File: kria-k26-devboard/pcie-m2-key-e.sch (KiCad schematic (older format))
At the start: 10 parts, among them P1 2199119-6

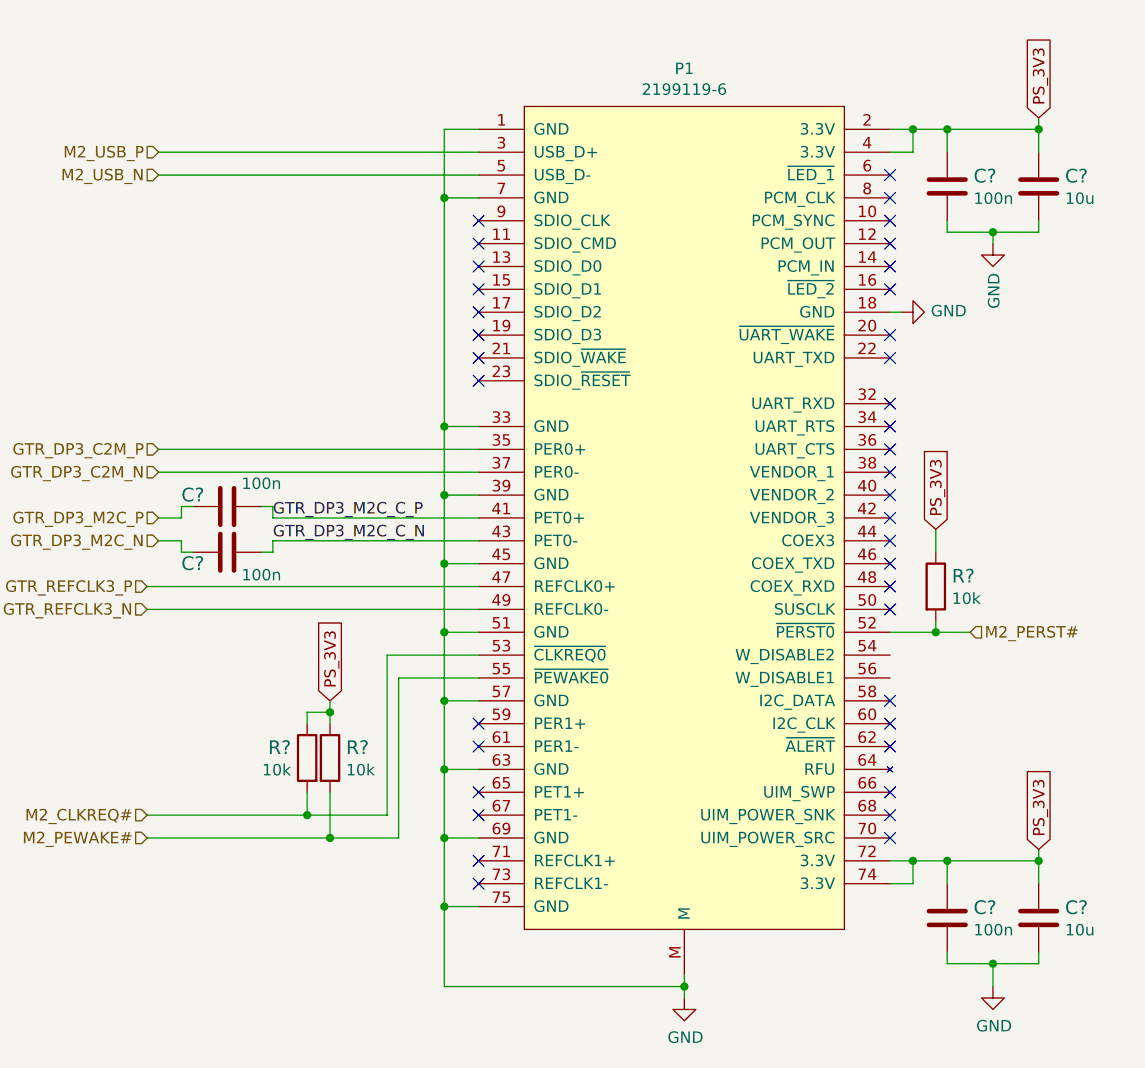
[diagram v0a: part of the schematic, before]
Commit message: Finished reset logic, added crystal gen. to USB PHY, create power toggle for SD 3.0
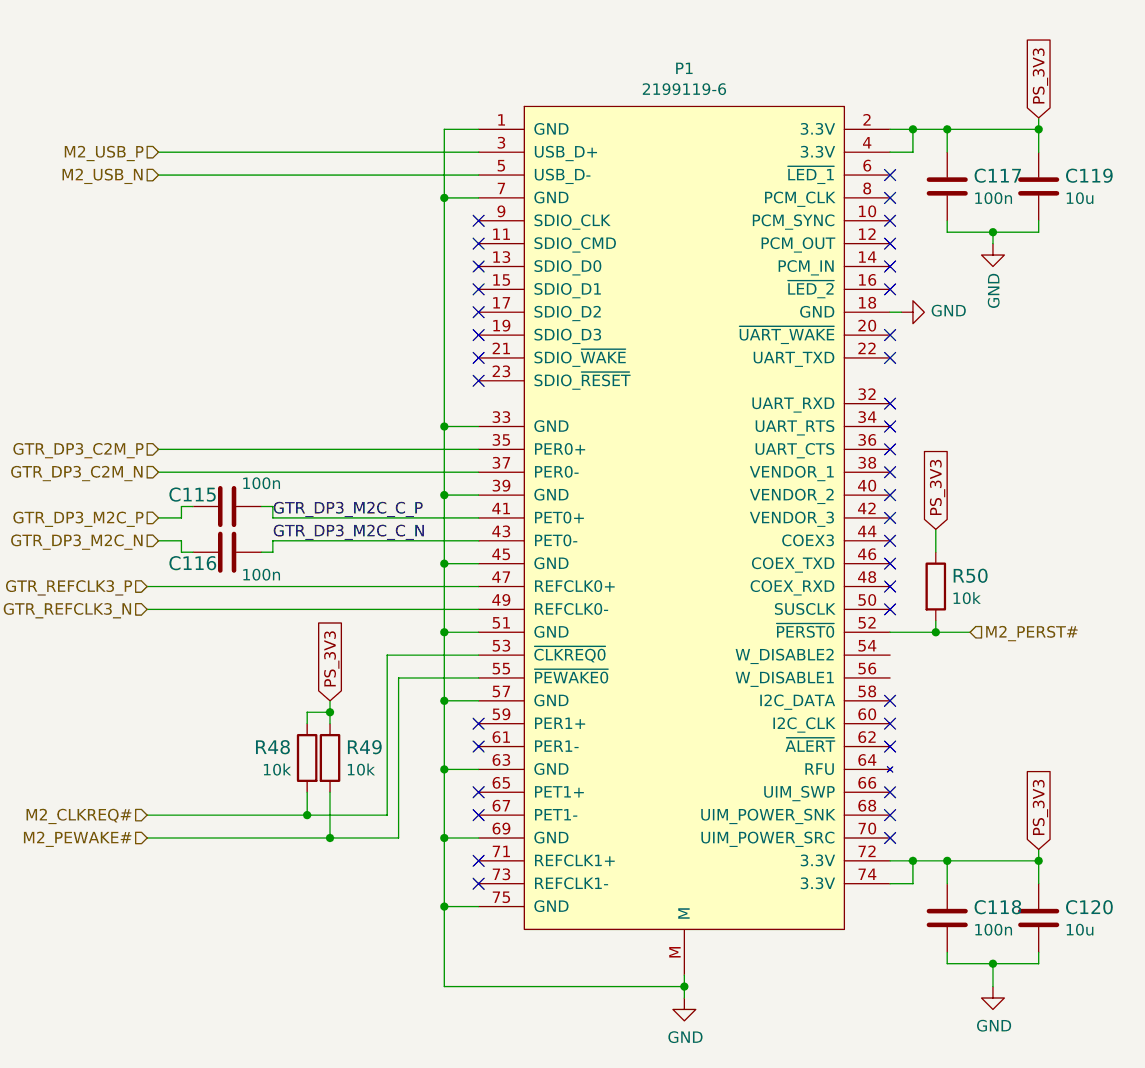
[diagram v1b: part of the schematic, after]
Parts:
- gave numbers to parts that had none: 9
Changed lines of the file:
@@
 Connection ~ 4950 5100
 $Comp
-L power:GND #PWR?
+L power:GND #PWR069
 U 1 1 65600FFC
 P 6000 5500
-F 0 "#PWR?" H 6000 5250 50  0001 C CNN
+F 0 "#PWR069" H 6000 5250 50  0001 C CNN
 F 1 "GND" H 6005 5327 50  0000 C CNN
 F 2 "" H 6000 5500 50  0001 C CNN
@@
 NoConn ~ 6900 4200
 $Comp
-L antmicroCapacitors0402:C_100n_0402 C?
+L antmicroCapacitors0402:C_100n_0402 C115
 U 1 1 65611557
 P 4000 3350
-F 0 "C?" V 3950 3200 60  0000 C CNN
+F 0 "C115" V 3950 3200 60  0000 C CNN
 F 1 "C_100n_0402" H 4000 3200 60  0001 C CNN
 F 2 "antmicro-footprints:0402-cap" H 4200 3550 60  0001 L CNN
@@
 $EndComp
 $Comp
-L antmicroCapacitors0402:C_100n_0402 C?
+L antmicroCapacitors0402:C_100n_0402 C116
 U 1 1 656118CD
 P 4000 3550
-F 0 "C?" V 3950 3400 60  0000 C CNN
+F 0 "C116" V 3950 3400 60  0000 C CNN
 F 1 "C_100n_0402" H 4000 3400 60  0001 C CNN
 F 2 "antmicro-footprints:0402-cap" H 4200 3750 60  0001 L CNN
@@
 PS_3V3
 $Comp
-L antmicroCapacitors0603:C_10u_0603 C?
+L antmicroCapacitors0603:C_10u_0603 C119
 U 1 1 65686406
 P 7550 1950
-F 0 "C?" H 7665 1995 60  0000 L CNN
+F 0 "C119" H 7665 1995 60  0000 L CNN
 F 1 "C_10u_0603" H 7550 1800 60  0001 C CNN
 F 2 "antmicro-footprints:0603-cap" H 7750 2150 60  0001 L CNN
@@
 PS_3V3
 $Comp
-L antmicroResistors0402:R_10k_0402 R?
+L antmicroResistors0402:R_10k_0402 R49
 U 1 1 6569DB94
 P 4450 4450
-F 0 "R?" V 4405 4520 60  0000 L CNN
+F 0 "R49" V 4405 4520 60  0000 L CNN
 F 1 "R_10k_0402" H 4450 4300 60  0001 C CNN
 F 2 "antmicro-footprints:0402-res" H 4650 4650 60  0001 L CNN
@@
 $EndComp
 $Comp
-L antmicroResistors0402:R_10k_0402 R?
+L antmicroResistors0402:R_10k_0402 R48
 U 1 1 6569F2E0
 P 4350 4450
-F 0 "R?" V 4305 4520 60  0000 L CNN
+F 0 "R48" V 4305 4520 60  0000 L CNN
 F 1 "R_10k_0402" H 4350 4300 60  0001 C CNN
 F 2 "antmicro-footprints:0402-res" H 4550 4650 60  0001 L CNN
@@
 M2_PEWAKE#
 $Comp
-L antmicroResistors0402:R_10k_0402 R?
+L antmicroResistors0402:R_10k_0402 R50
 U 1 1 656A5E34
 P 7100 3700
-F 0 "R?" V 7055 3770 60  0000 L CNN
+F 0 "R50" V 7055 3770 60  0000 L CNN
 F 1 "R_10k_0402" H 7100 3550 60  0001 C CNN
 F 2 "antmicro-footprints:0402-res" H 7300 3900 60  0001 L CNN
@@
 Connection ~ 7000 1700
 $Comp
-L antmicroCapacitors0402:C_100n_0402 C?
+L antmicroCapacitors0402:C_100n_0402 C117
 U 1 1 656D8EC8
 P 7150 1950
-F 0 "C?" H 7265 1995 60  0000 L CNN
+F 0 "C117" H 7265 1995 60  0000 L CNN
 F 1 "C_100n_0402" H 7150 1800 60  0001 C CNN
 F 2 "antmicro-footprints:0402-cap" H 7350 2150 60  0001 L CNN
@@
 PS_3V3
 $Comp
-L antmicroCapacitors0603:C_10u_0603 C?
+L antmicroCapacitors0603:C_10u_0603 C120
 U 1 1 656DBDBC
 P 7550 5150
-F 0 "C?" H 7665 5195 60  0000 L CNN
+F 0 "C120" H 7665 5195 60  0000 L CNN
 F 1 "C_10u_0603" H 7550 5000 60  0001 C CNN
 F 2 "antmicro-footprints:0603-cap" H 7750 5350 60  0001 L CNN
@@
 Connection ~ 7550 4900
 $Comp
-L power:GND #PWR?
+L power:GND #PWR072
 U 1 1 656DBDCA
 P 7350 5450
-F 0 "#PWR?" H 7350 5200 50  0001 C CNN
+F 0 "#PWR072" H 7350 5200 50  0001 C CNN
 F 1 "GND" H 7355 5277 50  0000 C CNN
 F 2 "" H 7350 5450 50  0001 C CNN
@@
 	7550 4900 7550 4850
 $Comp
-L antmicroCapacitors0402:C_100n_0402 C?
+L antmicroCapacitors0402:C_100n_0402 C118
 U 1 1 656DBDDE
 P 7150 5150
-F 0 "C?" H 7265 5195 60  0000 L CNN
+F 0 "C118" H 7265 5195 60  0000 L CNN
 F 1 "C_100n_0402" H 7150 5000 60  0001 C CNN
 F 2 "antmicro-footprints:0402-cap" H 7350 5350 60  0001 L CNN
@@
 Connection ~ 7150 1700
 $Comp
-L power:GND #PWR?
+L power:GND #PWR071
 U 1 1 656CB469
 P 7350 2200
-F 0 "#PWR?" H 7350 1950 50  0001 C CNN
+F 0 "#PWR071" H 7350 1950 50  0001 C CNN
 F 1 "GND" V 7355 2072 50  0000 R CNN
 F 2 "" H 7350 2200 50  0001 C CNN
@@
 	7350 2150 7550 2150
 $Comp
-L power:GND #PWR?
+L power:GND #PWR070
 U 1 1 657BC2E7
 P 6950 2500
-F 0 "#PWR?" H 6950 2250 50  0001 C CNN
+F 0 "#PWR070" H 6950 2250 50  0001 C CNN
 F 1 "GND" V 6955 2372 50  0000 R CNN
 F 2 "" H 6950 2500 50  0001 C CNN

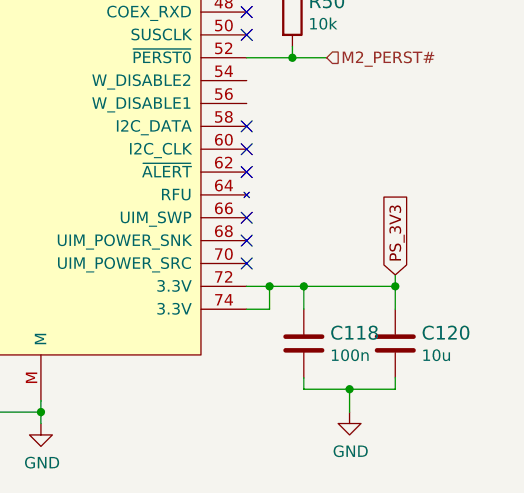
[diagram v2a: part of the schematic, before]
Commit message: Added second ETH interface, connect POE PSE
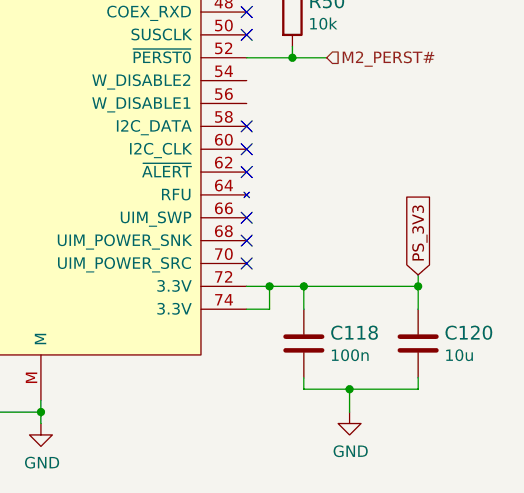
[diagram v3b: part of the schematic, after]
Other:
- moved on the sheet: C120
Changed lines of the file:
@@
 	1    0    0    -1
 $EndComp
-Text GLabel 7550 4850 1    50   Input ~ 0
+Text GLabel 7650 4850 1    50   Input ~ 0
 PS_3V3
 $Comp
 L antmicroCapacitors0603:C_10u_0603 C120
 U 1 1 656DBDBC
-P 7550 5150
-F 0 "C120" H 7665 5195 60  0000 L CNN
-F 1 "C_10u_0603" H 7550 5000 60  0001 C CNN
-F 2 "antmicro-footprints:0603-cap" H 7750 5350 60  0001 L CNN
-F 3 "" H 7550 5150 50  0001 C CNN
-F 4 "Murata" H 7750 5550 60  0001 L CNN "Manufacturer"
-F 5 "GRM188R61A106KE69D" H 7750 5450 60  0001 L CNN "MPN"
-F 6 "10u" H 7665 5097 50  0000 L CNN "Val"
-	1    7550 5150
+P 7650 5150
+F 0 "C120" H 7765 5195 60  0000 L CNN
+F 1 "C_10u_0603" H 7650 5000 60  0001 C CNN
+F 2 "antmicro-footprints:0603-cap" H 7850 5350 60  0001 L CNN
+F 3 "" H 7650 5150 50  0001 C CNN
+F 4 "Murata" H 7850 5550 60  0001 L CNN "Manufacturer"
+F 5 "GRM188R61A106KE69D" H 7850 5450 60  0001 L CNN "MPN"
+F 6 "10u" H 7765 5097 50  0000 L CNN "Val"
+	1    7650 5150
 	1    0    0    -1
 $EndComp
@@
 	7150 5000 7150 4900
 Wire Wire Line
-	7150 4900 7550 4900
+	7150 4900 7650 4900
 Wire Wire Line
-	7550 4900 7550 5000
-Connection ~ 7550 4900
+	7650 4900 7650 5000
+Connection ~ 7650 4900
 $Comp
 L power:GND #PWR072
@@
 	7150 5350 7350 5350
 Wire Wire Line
-	7550 5350 7550 5300
+	7650 5350 7650 5300
 Wire Wire Line
 	7350 5450 7350 5350
 Connection ~ 7350 5350
 Wire Wire Line
-	7350 5350 7550 5350
+	7350 5350 7650 5350
 Wire Wire Line
-	7550 4900 7550 4850
+	7650 4900 7650 4850
 $Comp
 L antmicroCapacitors0402:C_100n_0402 C118

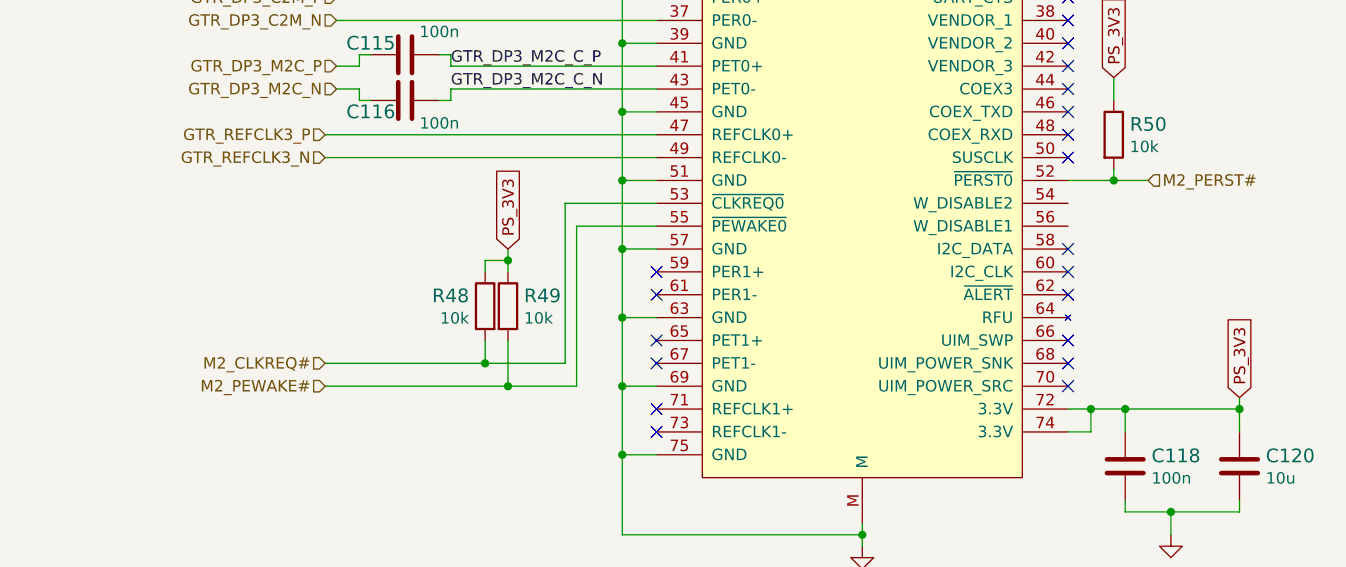
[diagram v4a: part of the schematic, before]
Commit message: fixed an issue with reset logic (Mixed PS and PL domain on OD buffer), extended the logic circuit to support M.2 PERST# (reset for PCIe WIFI), fixed the polarity of the camera control signal CAM_RST to comply with Antmicro standard, change CAM _SHDN to CAM_VSYNC, replaced the reset connector to fit additional signal M2_PERST
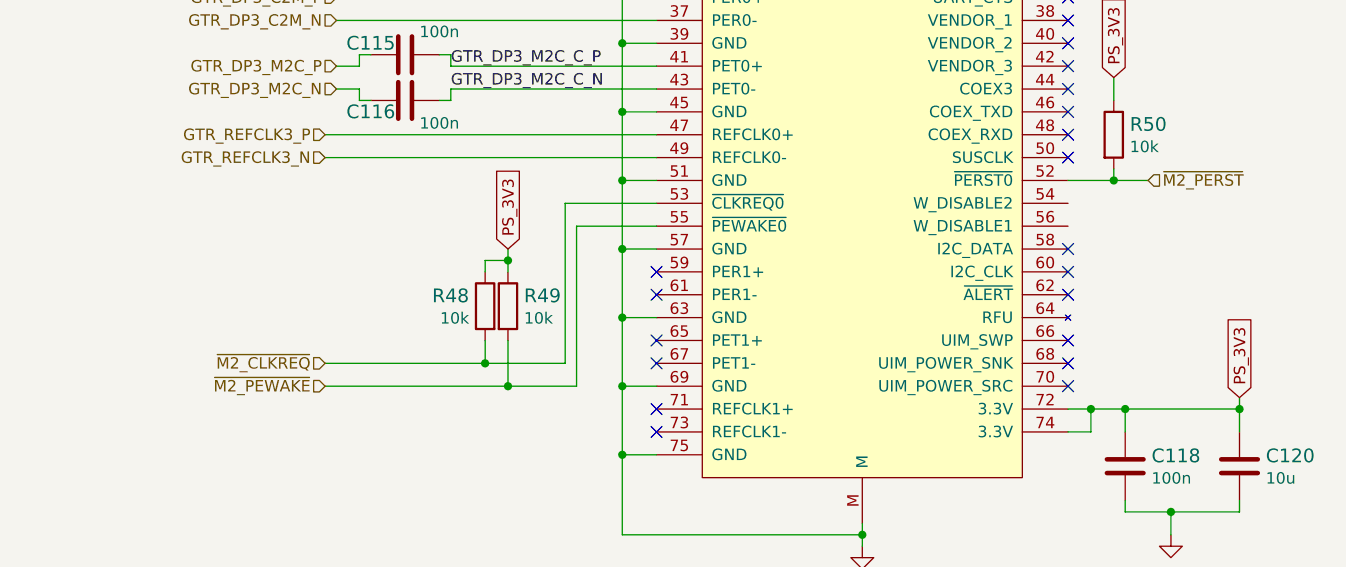
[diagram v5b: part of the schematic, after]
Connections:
- net M2_CLKREQ# renamed ~M2_CLKREQ
- net M2_PERST# renamed ~M2_PERST
- net M2_PEWAKE# renamed ~M2_PEWAKE
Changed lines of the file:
@@
 Wire Wire Line
 	4450 4600 4450 4800
-Text HLabel 3650 4700 0    50   Input ~ 0
-M2_CLKREQ#
 Text HLabel 3650 4800 0    50   Input ~ 0
-M2_PEWAKE#
+~M2_PEWAKE
 $Comp
 L antmicroResistors0402:R_10k_0402 R50
@@
 	7100 3550 7100 3450
 Text HLabel 7250 3900 2    50   Input ~ 0
-M2_PERST#
+~M2_PERST
 Wire Wire Line
 	7100 3900 7250 3900
@@
 	6000 5500 6000 5450
 Connection ~ 6000 5450
+Text HLabel 3650 4700 0    50   Input ~ 0
+~M2_CLKREQ
 $EndSCHEMATC

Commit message: Progress in PCB placement
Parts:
- renumbered C115 to C1, C116 to C2, C117 to C3, C118 to C4, C119 to C5, C120 to C6, R48 to R1, R49 to R2, R50 to R3
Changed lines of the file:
@@
 Connection ~ 4950 5100
 $Comp
-L power:GND #PWR069
+L power:GND #PWR01
 U 1 1 65600FFC
 P 6000 5500
-F 0 "#PWR069" H 6000 5250 50  0001 C CNN
+F 0 "#PWR01" H 6000 5250 50  0001 C CNN
 F 1 "GND" H 6005 5327 50  0000 C CNN
 F 2 "" H 6000 5500 50  0001 C CNN
@@
 NoConn ~ 6900 4200
 $Comp
-L antmicroCapacitors0402:C_100n_0402 C115
+L antmicroCapacitors0402:C_100n_0402 C1
 U 1 1 65611557
 P 4000 3350
-F 0 "C115" V 3950 3200 60  0000 C CNN
+F 0 "C1" V 3950 3200 60  0000 C CNN
 F 1 "C_100n_0402" H 4000 3200 60  0001 C CNN
 F 2 "antmicro-footprints:0402-cap" H 4200 3550 60  0001 L CNN
@@
 $EndComp
 $Comp
-L antmicroCapacitors0402:C_100n_0402 C116
+L antmicroCapacitors0402:C_100n_0402 C2
 U 1 1 656118CD
 P 4000 3550
-F 0 "C116" V 3950 3400 60  0000 C CNN
+F 0 "C2" V 3950 3400 60  0000 C CNN
 F 1 "C_100n_0402" H 4000 3400 60  0001 C CNN
 F 2 "antmicro-footprints:0402-cap" H 4200 3750 60  0001 L CNN
@@
 PS_3V3
 $Comp
-L antmicroCapacitors0603:C_10u_0603 C119
+L antmicroCapacitors0603:C_10u_0603 C5
 U 1 1 65686406
 P 7550 1950
-F 0 "C119" H 7665 1995 60  0000 L CNN
+F 0 "C5" H 7665 1995 60  0000 L CNN
 F 1 "C_10u_0603" H 7550 1800 60  0001 C CNN
 F 2 "antmicro-footprints:0603-cap" H 7750 2150 60  0001 L CNN
@@
 PS_3V3
 $Comp
-L antmicroResistors0402:R_10k_0402 R49
+L antmicroResistors0402:R_10k_0402 R2
 U 1 1 6569DB94
 P 4450 4450
-F 0 "R49" V 4405 4520 60  0000 L CNN
+F 0 "R2" V 4405 4520 60  0000 L CNN
 F 1 "R_10k_0402" H 4450 4300 60  0001 C CNN
 F 2 "antmicro-footprints:0402-res" H 4650 4650 60  0001 L CNN
@@
 $EndComp
 $Comp
-L antmicroResistors0402:R_10k_0402 R48
+L antmicroResistors0402:R_10k_0402 R1
 U 1 1 6569F2E0
 P 4350 4450
-F 0 "R48" V 4305 4520 60  0000 L CNN
+F 0 "R1" V 4305 4520 60  0000 L CNN
 F 1 "R_10k_0402" H 4350 4300 60  0001 C CNN
 F 2 "antmicro-footprints:0402-res" H 4550 4650 60  0001 L CNN
@@
 ~M2_PEWAKE
 $Comp
-L antmicroResistors0402:R_10k_0402 R50
+L antmicroResistors0402:R_10k_0402 R3
 U 1 1 656A5E34
 P 7100 3700
-F 0 "R50" V 7055 3770 60  0000 L CNN
+F 0 "R3" V 7055 3770 60  0000 L CNN
 F 1 "R_10k_0402" H 7100 3550 60  0001 C CNN
 F 2 "antmicro-footprints:0402-res" H 7300 3900 60  0001 L CNN
@@
 Connection ~ 7000 1700
 $Comp
-L antmicroCapacitors0402:C_100n_0402 C117
+L antmicroCapacitors0402:C_100n_0402 C3
 U 1 1 656D8EC8
 P 7150 1950
-F 0 "C117" H 7265 1995 60  0000 L CNN
+F 0 "C3" H 7265 1995 60  0000 L CNN
 F 1 "C_100n_0402" H 7150 1800 60  0001 C CNN
 F 2 "antmicro-footprints:0402-cap" H 7350 2150 60  0001 L CNN
@@
 PS_3V3
 $Comp
-L antmicroCapacitors0603:C_10u_0603 C120
+L antmicroCapacitors0603:C_10u_0603 C6
 U 1 1 656DBDBC
 P 7650 5150
-F 0 "C120" H 7765 5195 60  0000 L CNN
+F 0 "C6" H 7765 5195 60  0000 L CNN
 F 1 "C_10u_0603" H 7650 5000 60  0001 C CNN
 F 2 "antmicro-footprints:0603-cap" H 7850 5350 60  0001 L CNN
@@
 Connection ~ 7650 4900
 $Comp
-L power:GND #PWR072
+L power:GND #PWR04
 U 1 1 656DBDCA
 P 7350 5450
-F 0 "#PWR072" H 7350 5200 50  0001 C CNN
+F 0 "#PWR04" H 7350 5200 50  0001 C CNN
 F 1 "GND" H 7355 5277 50  0000 C CNN
 F 2 "" H 7350 5450 50  0001 C CNN
@@
 	7650 4900 7650 4850
 $Comp
-L antmicroCapacitors0402:C_100n_0402 C118
+L antmicroCapacitors0402:C_100n_0402 C4
 U 1 1 656DBDDE
 P 7150 5150
-F 0 "C118" H 7265 5195 60  0000 L CNN
+F 0 "C4" H 7265 5195 60  0000 L CNN
 F 1 "C_100n_0402" H 7150 5000 60  0001 C CNN
 F 2 "antmicro-footprints:0402-cap" H 7350 5350 60  0001 L CNN
@@
 Connection ~ 7150 1700
 $Comp
-L power:GND #PWR071
+L power:GND #PWR03
 U 1 1 656CB469
 P 7350 2200
-F 0 "#PWR071" H 7350 1950 50  0001 C CNN
+F 0 "#PWR03" H 7350 1950 50  0001 C CNN
 F 1 "GND" V 7355 2072 50  0000 R CNN
 F 2 "" H 7350 2200 50  0001 C CNN
@@
 	7350 2150 7550 2150
 $Comp
-L power:GND #PWR070
+L power:GND #PWR02
 U 1 1 657BC2E7
 P 6950 2500
-F 0 "#PWR070" H 6950 2250 50  0001 C CNN
+F 0 "#PWR02" H 6950 2250 50  0001 C CNN
 F 1 "GND" V 6955 2372 50  0000 R CNN
 F 2 "" H 6950 2500 50  0001 C CNN

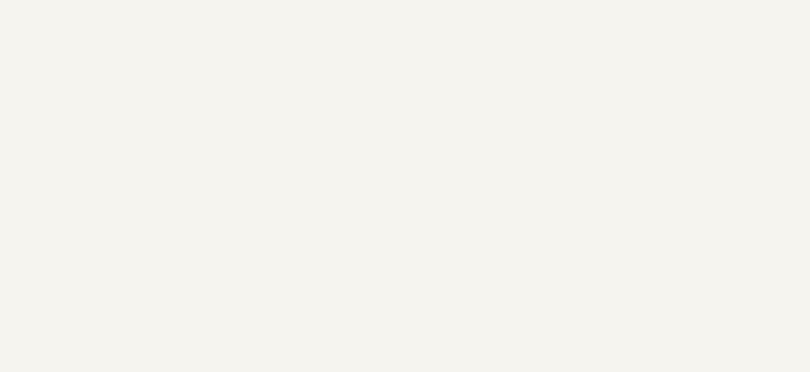
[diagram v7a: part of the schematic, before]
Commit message: Initial routing of ETH and USB 2.0 interface, debug socket USB replaced to USB-C, added stud for M2
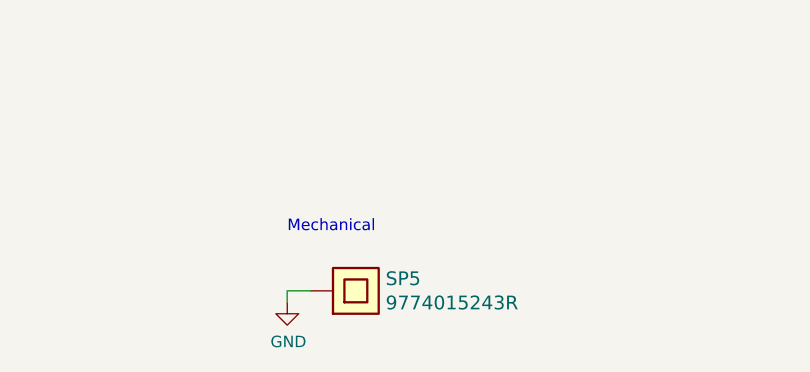
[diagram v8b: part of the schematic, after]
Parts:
- added SP5: 9774015243R, antmicro-footprints:9774015243R, symbol antmicroMechanicalParts:9774015243R
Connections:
- net GND: now also SP5.1
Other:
- note added: "Mechanical"
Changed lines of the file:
@@
 Text HLabel 3650 4700 0    50   Input ~ 0
 ~M2_CLKREQ
+$Comp
+L power:GND #PWR0307
+U 1 1 6256A4FD
+P 5600 7200
+F 0 "#PWR0307" H 5600 6950 50  0001 C CNN
+F 1 "GND" H 5605 7027 50  0000 C CNN
+F 2 "" H 5600 7200 50  0001 C CNN
+F 3 "" H 5600 7200 50  0001 C CNN
+	1    5600 7200
+	1    0    0    -1
+$EndComp
+Wire Wire Line
+	5700 7150 5600 7150
+Wire Wire Line
+	5600 7150 5600 7200
+Text Notes 5600 6900 0    50   ~ 0
+Mechanical
+$Comp
+L antmicroMechanicalParts:9774015243R SP5
+U 1 1 62573850
+P 5900 7150
+F 0 "SP5" H 6030 7203 60  0000 L CNN
+F 1 "9774015243R" H 6030 7097 60  0000 L CNN
+F 2 "antmicro-footprints:9774015243R" H 5900 7150 60  0001 C CNN
+F 3 "https://www.we-online.com/catalog/datasheet/9774015243R.pdf" H 5900 7150 60  0001 C CNN
+F 4 "Wurth Elektronik" H 5900 7150 50  0001 C CNN "Manufacturer"
+F 5 "9774015243R" H 5900 7150 50  0001 C CNN "MPN"
+	1    5900 7150
+	1    0    0    -1
+$EndComp
 $EndSCHEMATC
